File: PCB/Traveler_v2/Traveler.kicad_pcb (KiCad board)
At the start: 2 copper layers, 65 x 72.5 mm, 40 parts, among them J1 Conn_01x06_motFL, J2 Conn_01x06_motFR, J3 Conn_01x06_motBL, J4 Conn_01x06_motBR, J5 Conn_batt, U1 ESP32-DEVKITC, U2 12v-5v, U4 DRV8411APWPR, U5 DRV8411APWPR

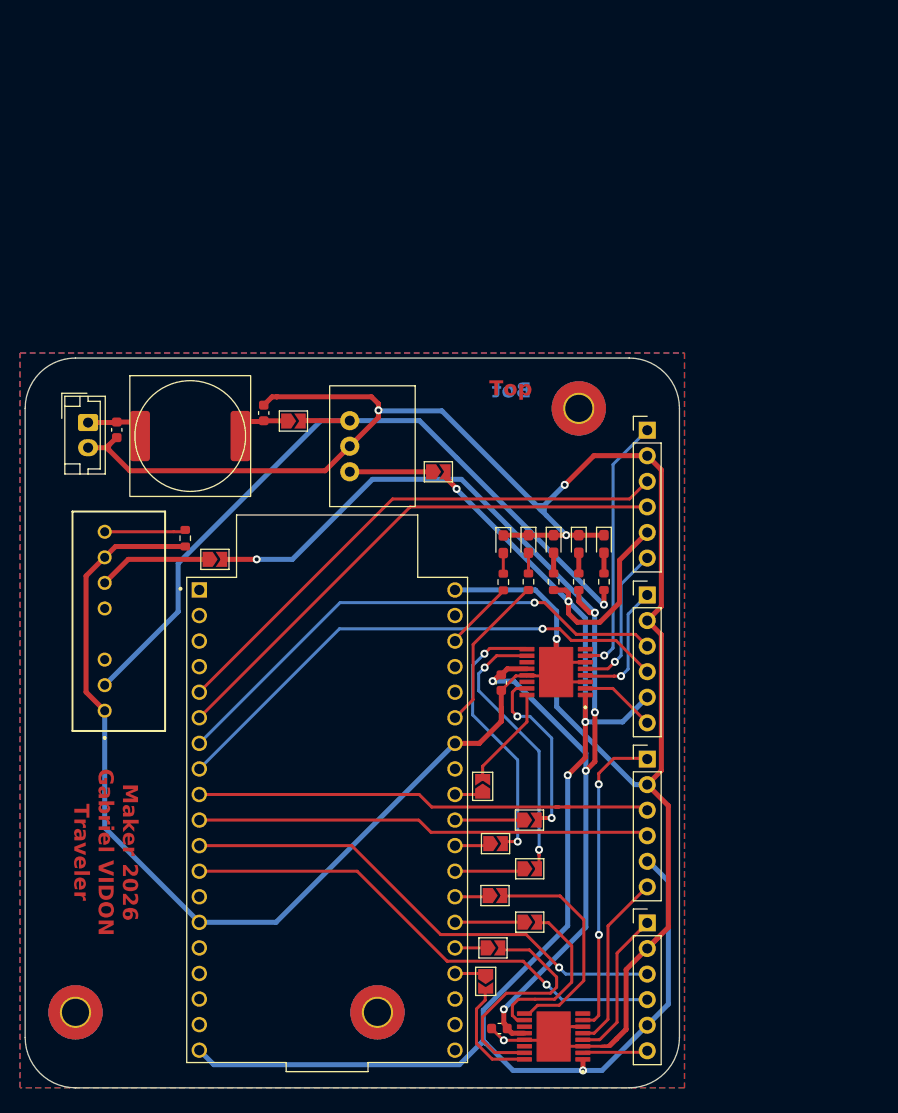
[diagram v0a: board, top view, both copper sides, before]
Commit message: Finition PCB et envoi vers fabrication
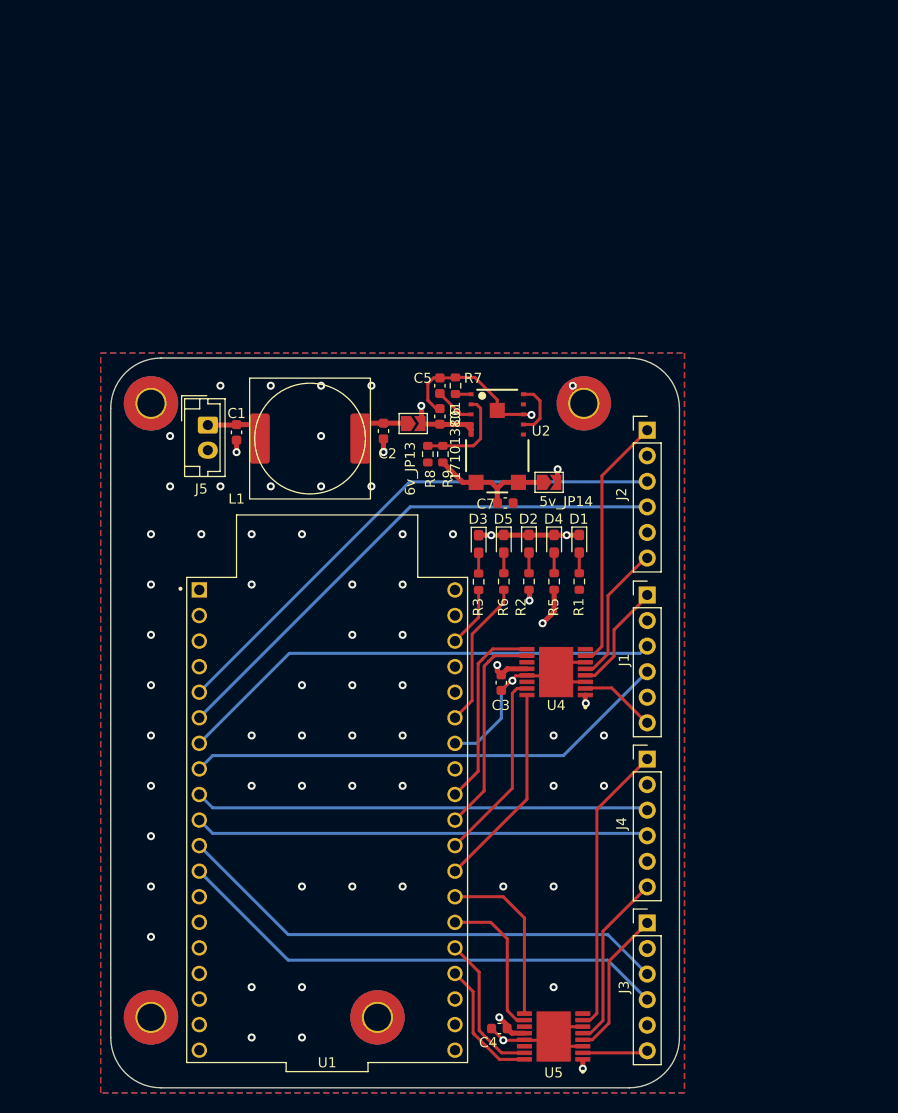
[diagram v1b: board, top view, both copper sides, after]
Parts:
- removed 6v_JP15, A1IN1_JP5, A1IN2_JP6, A2IN1_JP9, A2IN2_JP10, B1IN1_JP7, B1IN2_JP8, B2IN1_JP11, B2IN2_JP12: SolderJumper_2_Open, Jumper:SolderJumper-2_P1.3mm_Open_TrianglePad1.0x1.5mm
- removed PS1: 17791063215, 17791063215:17791063215
- removed R4: 21.5k, Resistor_SMD:R_0603_1608Metric
- added C5: 1u, Capacitor_SMD:C_0603_1608Metric, F.Cu at (158.7, 45.2)
- added C6: 4.7u, Capacitor_SMD:C_0603_1608Metric, F.Cu at (158.7, 48.3)
- added C7: C, Capacitor_SMD:C_0603_1608Metric, F.Cu at (165.2, 56.9)
- added H4: MountingHole_Pad, MountingHole:MountingHole_2.7mm_Pad_TopBottom, F.Cu at (130.0, 108.0)
- added R7: 5.6k, Resistor_SMD:R_0603_1608Metric, F.Cu at (160.2, 45.2)
- added R8: 330k, Resistor_SMD:R_0603_1608Metric, F.Cu at (159.0, 52.0)
- added R9: 1.5M, Resistor_SMD:R_0603_1608Metric, F.Cu at (157.5, 52.0)
- U2: value 12v-5v -> 171013801; footprint Conv_dc-dc:173950x78 -> 171013801:WPME-VDLM_LGA-12EP
- moved H2 61.0 mm to (130.0, 47.0)
- moved C2 12.0 mm to (153.1, 49.8), turned to -90 degrees
- moved 6v_JP13 11.9 mm to (156.1, 49.0)
- moved C1 11.9 mm to (138.5, 49.9)
- moved J5 11.9 mm to (135.7, 49.2)
- moved L1 11.9 mm to (145.8, 50.5)
- moved 5v_JP14 11.1 mm to (169.6, 54.9)
- moved U2 4.68 mm to (164.4, 50.8)
- moved D1 2.45 mm to (172.5, 61.0)
- moved D2 2.45 mm to (167.5, 60.9)
- moved D3 2.45 mm to (162.5, 61.0)
- moved D4 2.45 mm to (170.0, 61.0)
- moved D5 2.45 mm to (165.0, 60.9)
- moved R1 2.45 mm to (172.6, 64.7)
- moved R2 2.45 mm to (167.5, 64.7)
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- renumbered 12v_JP13 to 6v_JP13
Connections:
- 5v_JP14 pad 1: Net-(5v_JP14-A) -> Vout
- 6v_JP13 pad 2: 12V -> 6V
- U1 pad 23: Net-(A2IN1_JP9-A) -> A2IN1
- U1 pad 24: Net-(A2IN2_JP10-A) -> A2IN2
- U1 pad 25: Net-(B2IN2_JP12-A) -> B2IN2
- U1 pad 26: Net-(B2IN1_JP11-A) -> B2IN1
- U1 pad 27: Net-(B1IN2_JP8-A) -> A1IN1
- U1 pad 28: Net-(B1IN1_JP7-A) -> A1IN2
- U1 pad 29: Net-(A1IN2_JP6-A) -> B1IN2
- U1 pad 30: Net-(A1IN1_JP5-A) -> B1IN1
- U2 pad 1: 12V -> Net-(U2-FSW)
- U2 pad 2: GND -> Net-(U2-FB)
- U2 pad 3: Net-(5v_JP14-A) -> Net-(U2-Vcc)
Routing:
- net GND: track 323.9 -> 64.6 mm, vias 5 -> 63
- net 12V: track 77.1 -> 0.00 mm, vias 1 -> 0
- net 5V: track 163.3 -> 130.2 mm, vias 5 -> 4
- net 6V: track 114.0 -> 88.7 mm, vias 6 -> 4
- net Vout: track 0.00 -> 12.6 mm
- net Net-(6v_JP15-A): track 11.2 -> 0.00 mm
- net A1IN1: track 10.2 -> 20.5 mm
- net Net-(U2-FB): track 0.00 -> 9.67 mm
- net A2IN2: track 23.1 -> 14.6 mm
- net Net-(PS1-FB): track 8.12 -> 0.00 mm
- net Net-(5v_JP14-A): track 8.07 -> 0.00 mm
- net B1IN1: track 27.0 -> 19.4 mm, vias 2 -> 0
- net Net-(A1IN2_JP6-A): track 7.13 -> 0.00 mm
- net Net-(B1IN2_JP8-A): track 6.90 -> 0.00 mm
- net Net-(B2IN2_JP12-A): track 6.71 -> 0.00 mm
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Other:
- board size 65 x 72.5 mm -> 56.5 x 72.5 mm
- copper layers 2 -> 4
- board text removed: "Bot"
- board text removed: "Maker 2026 Gabriel VIDON Traveler"
- board text removed: "Top"

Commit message: erreur avec le ldo, ordre des pins inversé sur KiCad, composant à souder en araignée
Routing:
- net GND: vias 63 -> 62
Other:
- board text added: "Pin order reversed, check datasheet"
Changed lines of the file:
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@@
 		(layer "Edge.Cuts")
+	)
+	(gr_text "Pin order reversed, check datasheet"
+		(at 165.9 46.5 45)
+		(layer "F.SilkS")
+		(effects
+			(font
+				(size 1.5 1.5)
+				(thickness 0.3)
+				(bold yes)
+			)
+			(justify left bottom)
+		)
 	)
 	(segment
@@
 		(size 0.8)
 		(drill 0.4)
-		(layers "F.Cu" "B.Cu")
-		(free yes)
-		(net 21)
-	)
-	(via
-		(at 171.9 45.25)
-		(size 0.8)
-		(drill 0.4)

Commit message: Code moteurs
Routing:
- net GND: track 64.6 -> 63.8 mm, vias 62 -> 61
